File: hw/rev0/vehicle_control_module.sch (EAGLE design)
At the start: 486 parts, among them IC1 SJA1105TELY, IC10 TJA1100HNZ, IC11 KSZ8061MNXI-TR, IC12 TJA1100HNZ, IC13 TLE9250XSJXUMA1, IC17 LP5907QMFX-3.3Q1, IC18 TLE9250XSJXUMA1, IC2 ATSAMV71Q21B-AABT, IC3 TJA1100HNZ, IC4 FT2232HL, IC5 TRS3232EQPWRQ1, IC6 SST26VF032BT-104I_SM, IC7 DS3231SN#, IC8 74HC7541D-Q100J, IC9 TPS62242DRVR, J10 5-2337992-3, J11 2301843-1, J12 1017505, J13 2301843-1, J15 693022010811, J2 2305018-2, J27 2041119-2, J3 1017505, J4 1017505, J5 1017505, J6 1017505, J7 1017505, J8 1017505, J9 1017505, U1 122-2920-GR, U2 LM63625, U3 TPS62007-Q1_DGS_10, Y1 NX3225SA-25MHZ-EXS00A-CS11338, Y3 ABM8AIG-12.000MHZ-1Z-T

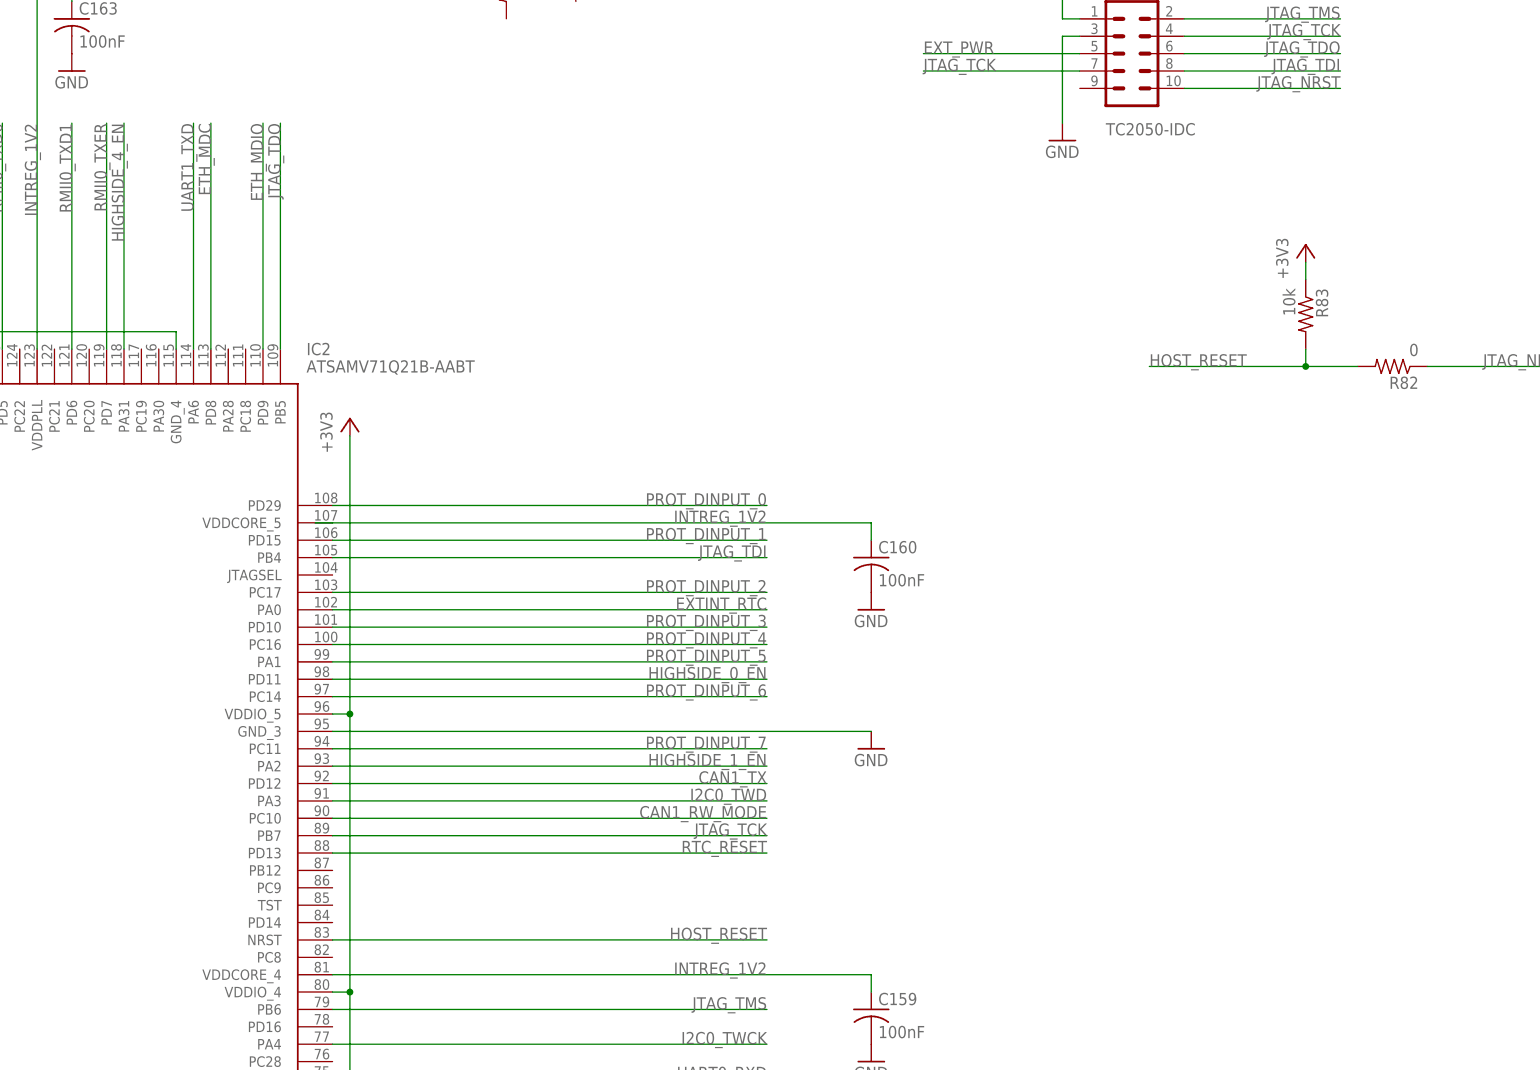
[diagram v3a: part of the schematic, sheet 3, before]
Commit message: Add Debug LEDs
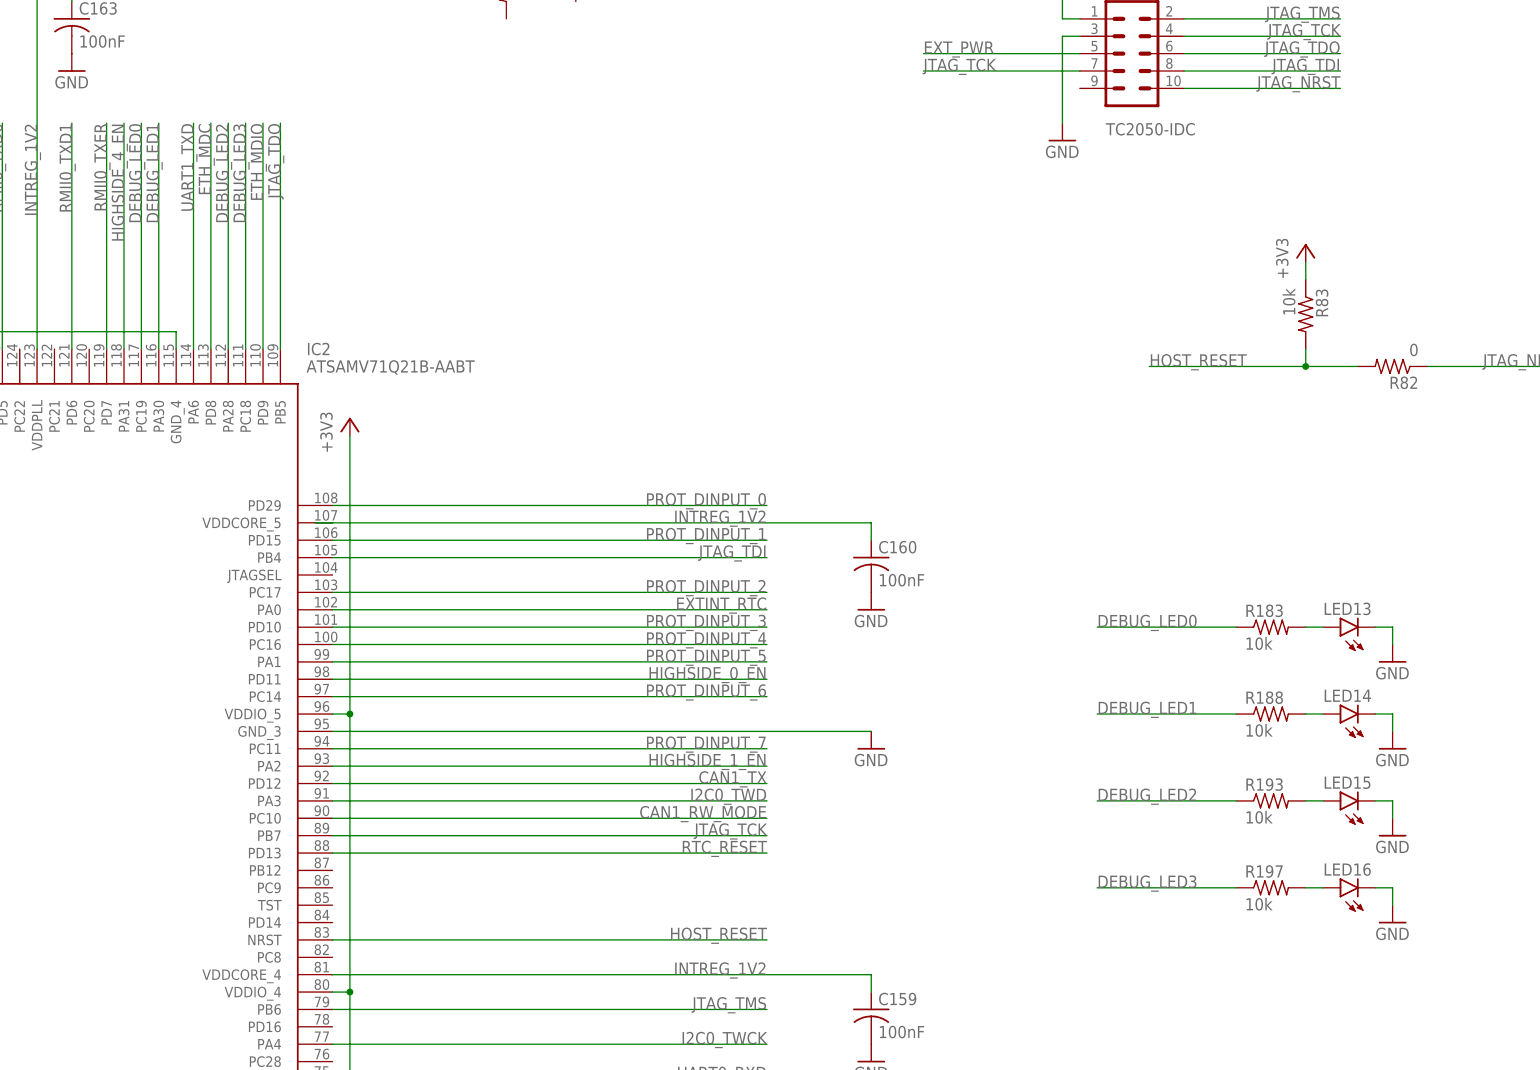
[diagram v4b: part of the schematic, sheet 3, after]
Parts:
- added LED13, LED14, LED15, LED16: (no value), led:LEDCHIPLED_0603
- added R183, R188, R193, R197: 10k, rcl:R-US_R0603
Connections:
- new net DEBUG_LED0: IC2.PC19, R183.1
- new net DEBUG_LED1: IC2.PA30, R188.1
- new net DEBUG_LED2: IC2.PA28, R193.1
- new net DEBUG_LED3: IC2.PC18, R197.1
- new net N$156: LED15.A, R193.2
- new net N$157: LED16.A, R197.2
- new net N$22: LED13.A, R183.2
- new net N$23: LED14.A, R188.2
- net GND: now also LED13.C, LED14.C, LED15.C, LED16.C
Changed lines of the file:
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@@
 <part name="VDD6" library="supply1" library_urn="urn:adsk.eagle:library:371" deviceset="VDD" device="" value="+1V2"/>
 <part name="VDD7" library="supply1" library_urn="urn:adsk.eagle:library:371" deviceset="VDD" device="" value="+1V2"/>
+<part name="R183" library="rcl" library_urn="urn:adsk.eagle:library:334" deviceset="R-US_" device="R0603" package3d_urn="urn:adsk.eagle:package:23555/3" value="10k"/>
+<part name="LED13" library="led" library_urn="urn:adsk.eagle:library:259" deviceset="LED" device="CHIPLED_0603" package3d_urn="urn:adsk.eagle:package:15822/2"/>
+<part name="GND46" library="supply1" library_urn="urn:adsk.eagle:library:371" deviceset="GND" device=""/>
+<part name="R188" library="rcl" library_urn="urn:adsk.eagle:library:334" deviceset="R-US_" device="R0603" package3d_urn="urn:adsk.eagle:package:23555/3" value="10k"/>
+<part name="LED14" library="led" library_urn="urn:adsk.eagle:library:259" deviceset="LED" device="CHIPLED_0603" package3d_urn="urn:adsk.eagle:package:15822/2"/>
+<part name="GND47" library="supply1" library_urn="urn:adsk.eagle:library:371" deviceset="GND" device=""/>
+<part name="R193" library="rcl" library_urn="urn:adsk.eagle:library:334" deviceset="R-US_" device="R0603" package3d_urn="urn:adsk.eagle:package:23555/3" value="10k"/>
+<part name="LED15" library="led" library_urn="urn:adsk.eagle:library:259" deviceset="LED" device="CHIPLED_0603" package3d_urn="urn:adsk.eagle:package:15822/2"/>
+<part name="GND48" library="supply1" library_urn="urn:adsk.eagle:library:371" deviceset="GND" device=""/>
+<part name="R197" library="rcl" library_urn="urn:adsk.eagle:library:334" deviceset="R-US_" device="R0603" package3d_urn="urn:adsk.eagle:package:23555/3" value="10k"/>
+<part name="LED16" library="led" library_urn="urn:adsk.eagle:library:259" deviceset="LED" device="CHIPLED_0603" package3d_urn="urn:adsk.eagle:package:15822/2"/>
+<part name="GND49" library="supply1" library_urn="urn:adsk.eagle:library:371" deviceset="GND" device=""/>
 </parts>
 <sheets>
@@
 <attribute name="VALUE" x="93.98" y="68.58" size="1.778" layer="96"/>
 </instance>
+<instance part="R183" gate="G$1" x="350.52" y="157.48" smashed="yes">
+<attribute name="NAME" x="346.71" y="158.9786" size="1.778" layer="95"/>
+<attribute name="VALUE" x="346.71" y="154.178" size="1.778" layer="96"/>
+</instance>
+<instance part="LED13" gate="G$1" x="360.68" y="157.48" smashed="yes" rot="R90">
+<attribute name="NAME" x="365.252" y="161.036" size="1.778" layer="95" rot="R180"/>
+<attribute name="VALUE" x="365.252" y="163.195" size="1.778" layer="96" rot="R180"/>
+</instance>
+<instance part="GND46" gate="1" x="368.3" y="152.4" smashed="yes">
+<attribute name="VALUE" x="365.76" y="149.86" size="1.778" layer="96"/>
+</instance>
+<instance part="R188" gate="G$1" x="350.52" y="144.78" smashed="yes">
+<attribute name="NAME" x="346.71" y="146.2786" size="1.778" layer="95"/>
+<attribute name="VALUE" x="346.71" y="141.478" size="1.778" layer="96"/>
+</instance>
+<instance part="LED14" gate="G$1" x="360.68" y="144.78" smashed="yes" rot="R90">
+<attribute name="NAME" x="365.252" y="148.336" size="1.778" layer="95" rot="R180"/>
+<attribute name="VALUE" x="365.252" y="150.495" size="1.778" layer="96" rot="R180"/>
+</instance>
+<instance part="GND47" gate="1" x="368.3" y="139.7" smashed="yes">
+<attribute name="VALUE" x="365.76" y="137.16" size="1.778" layer="96"/>
+</instance>
+<instance part="R193" gate="G$1" x="350.52" y="132.08" smashed="yes">
+<attribute name="NAME" x="346.71" y="133.5786" size="1.778" layer="95"/>
+<attribute name="VALUE" x="346.71" y="128.778" size="1.778" layer="96"/>
+</instance>
+<instance part="LED15" gate="G$1" x="360.68" y="132.08" smashed="yes" rot="R90">
+<attribute name="NAME" x="365.252" y="135.636" size="1.778" layer="95" rot="R180"/>
+<attribute name="VALUE" x="365.252" y="137.795" size="1.778" layer="96" rot="R180"/>
+</instance>
+<instance part="GND48" gate="1" x="368.3" y="127" smashed="yes">
+<attribute name="VALUE" x="365.76" y="124.46" size="1.778" layer="96"/>
+</instance>
+<instance part="R197" gate="G$1" x="350.52" y="119.38" smashed="yes">
+<attribute name="NAME" x="346.71" y="120.8786" size="1.778" layer="95"/>
+<attribute name="VALUE" x="346.71" y="116.078" size="1.778" layer="96"/>
+</instance>
+<instance part="LED16" gate="G$1" x="360.68" y="119.38" smashed="yes" rot="R90">
+<attribute name="NAME" x="365.252" y="122.936" size="1.778" layer="95" rot="R180"/>
+<attribute name="VALUE" x="365.252" y="125.095" size="1.778" layer="96" rot="R180"/>
+</instance>
+<instance part="GND49" gate="1" x="368.3" y="114.3" smashed="yes">
+<attribute name="VALUE" x="365.76" y="111.76" size="1.778" layer="96"/>
+</instance>
 </instances>
 <busses>
@@
 <pinref part="GND312" gate="1" pin="GND"/>
 </segment>
+<segment>
+<pinref part="LED13" gate="G$1" pin="C"/>
+<pinref part="GND46" gate="1" pin="GND"/>
+<wire x1="365.76" y1="157.48" x2="368.3" y2="157.48" width="0.1524" layer="91"/>
+<wire x1="368.3" y1="157.48" x2="368.3" y2="154.94" width="0.1524" layer="91"/>
+</segment>
+<segment>
+<pinref part="LED14" gate="G$1" pin="C"/>
+<pinref part="GND47" gate="1" pin="GND"/>
+<wire x1="365.76" y1="144.78" x2="368.3" y2="144.78" width="0.1524" layer="91"/>
+<wire x1="368.3" y1="144.78" x2="368.3" y2="142.24" width="0.1524" layer="91"/>
+</segment>
+<segment>
+<pinref part="LED15" gate="G$1" pin="C"/>
+<pinref part="GND48" gate="1" pin="GND"/>
+<wire x1="365.76" y1="132.08" x2="368.3" y2="132.08" width="0.1524" layer="91"/>
+<wire x1="368.3" y1="132.08" x2="368.3" y2="129.54" width="0.1524" layer="91"/>
+</segment>
+<segment>
+<pinref part="LED16" gate="G$1" pin="C"/>
+<pinref part="GND49" gate="1" pin="GND"/>
+<wire x1="365.76" y1="119.38" x2="368.3" y2="119.38" width="0.1524" layer="91"/>
+<wire x1="368.3" y1="119.38" x2="368.3" y2="116.84" width="0.1524" layer="91"/>
+</segment>
 </net>
 <net name="EXT_PWR" class="0">
@@
 </segment>
 </net>
+<net name="N$22" class="0">
+<segment>
+<pinref part="R183" gate="G$1" pin="2"/>
+<pinref part="LED13" gate="G$1" pin="A"/>
+<wire x1="355.6" y1="157.48" x2="358.14" y2="157.48" width="0.1524" layer="91"/>
+</segment>
+</net>
+<net name="DEBUG_LED0" class="0">
+<segment>
+<pinref part="R183" gate="G$1" pin="1"/>
+<wire x1="345.44" y1="157.48" x2="325.12" y2="157.48" width="0.1524" layer="91"/>
+<label x="325.12" y="157.48" size="1.778" layer="95"/>
+</segment>
+<segment>
+<pinref part="IC2" gate="G$1" pin="PC19"/>
+<wire x1="185.42" y1="198.12" x2="185.42" y2="231.14" width="0.1524" layer="91"/>
+<label x="185.42" y="231.14" size="1.778" layer="95" rot="MR270"/>
+</segment>
+</net>
+<net name="N$23" class="0">
+<segment>
+<pinref part="R188" gate="G$1" pin="2"/>
+<pinref part="LED14" gate="G$1" pin="A"/>
+<wire x1="355.6" y1="144.78" x2="358.14" y2="144.78" width="0.1524" layer="91"/>
+</segment>
+</net>
+<net name="N$156" class="0">
+<segment>
+<pinref part="R193" gate="G$1" pin="2"/>
+<pinref part="LED15" gate="G$1" pin="A"/>
+<wire x1="355.6" y1="132.08" x2="358.14" y2="132.08" width="0.1524" layer="91"/>
+</segment>
+</net>
+<net name="N$157" class="0">
+<segment>
+<pinref part="R197" gate="G$1" pin="2"/>
+<pinref part="LED16" gate="G$1" pin="A"/>
+<wire x1="355.6" y1="119.38" x2="358.14" y2="119.38" width="0.1524" layer="91"/>
+</segment>
+</net>
+<net name="DEBUG_LED1" class="0">
+<segment>
+<pinref part="R188" gate="G$1" pin="1"/>
+<wire x1="345.44" y1="144.78" x2="325.12" y2="144.78" width="0.1524" layer="91"/>
+<label x="325.12" y="144.78" size="1.778" layer="95"/>
+</segment>
+<segment>
+<pinref part="IC2" gate="G$1" pin="PA30"/>
+<wire x1="187.96" y1="198.12" x2="187.96" y2="231.14" width="0.1524" layer="91"/>
+<label x="187.96" y="231.14" size="1.778" layer="95" rot="MR270"/>
+</segment>
+</net>
+<net name="DEBUG_LED2" class="0">
+<segment>
+<pinref part="R193" gate="G$1" pin="1"/>
+<wire x1="345.44" y1="132.08" x2="325.12" y2="132.08" width="0.1524" layer="91"/>
+<label x="325.12" y="132.08" size="1.778" layer="95"/>
+</segment>
+<segment>
+<pinref part="IC2" gate="G$1" pin="PA28"/>
+<wire x1="198.12" y1="198.12" x2="198.12" y2="231.14" width="0.1524" layer="91"/>
+<label x="198.12" y="231.14" size="1.778" layer="95" rot="MR270"/>
+</segment>
+</net>
+<net name="DEBUG_LED3" class="0">
+<segment>
+<pinref part="R197" gate="G$1" pin="1"/>
+<wire x1="345.44" y1="119.38" x2="325.12" y2="119.38" width="0.1524" layer="91"/>
+<label x="325.12" y="119.38" size="1.778" layer="95"/>
+</segment>
+<segment>
+<pinref part="IC2" gate="G$1" pin="PC18"/>
+<wire x1="200.66" y1="198.12" x2="200.66" y2="231.14" width="0.1524" layer="91"/>
+<label x="200.66" y="231.14" size="1.778" layer="95" rot="MR270"/>
+</segment>
+</net>
